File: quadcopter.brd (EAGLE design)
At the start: 138 x 138 mm, 65 parts, among them J1 AVR_SPI_PRG_6NS, Q1 N-CHANNEL_MOSFET, Q2 N-CHANNEL_MOSFET, Q3 N-CHANNEL_MOSFET, Q4 N-CHANNEL_MOSFET, U1 ATMEGA128RFA1

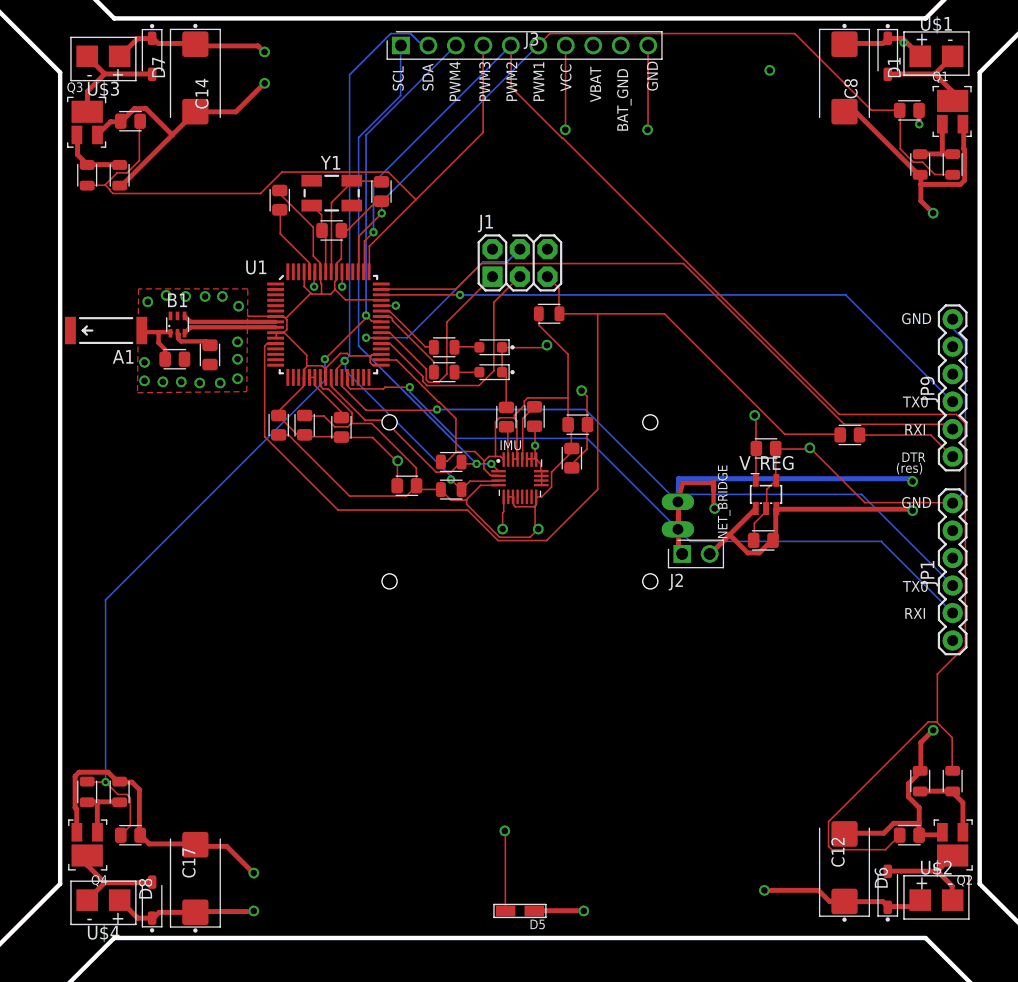
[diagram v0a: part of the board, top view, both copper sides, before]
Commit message: Changed ground on LED to batgnd"
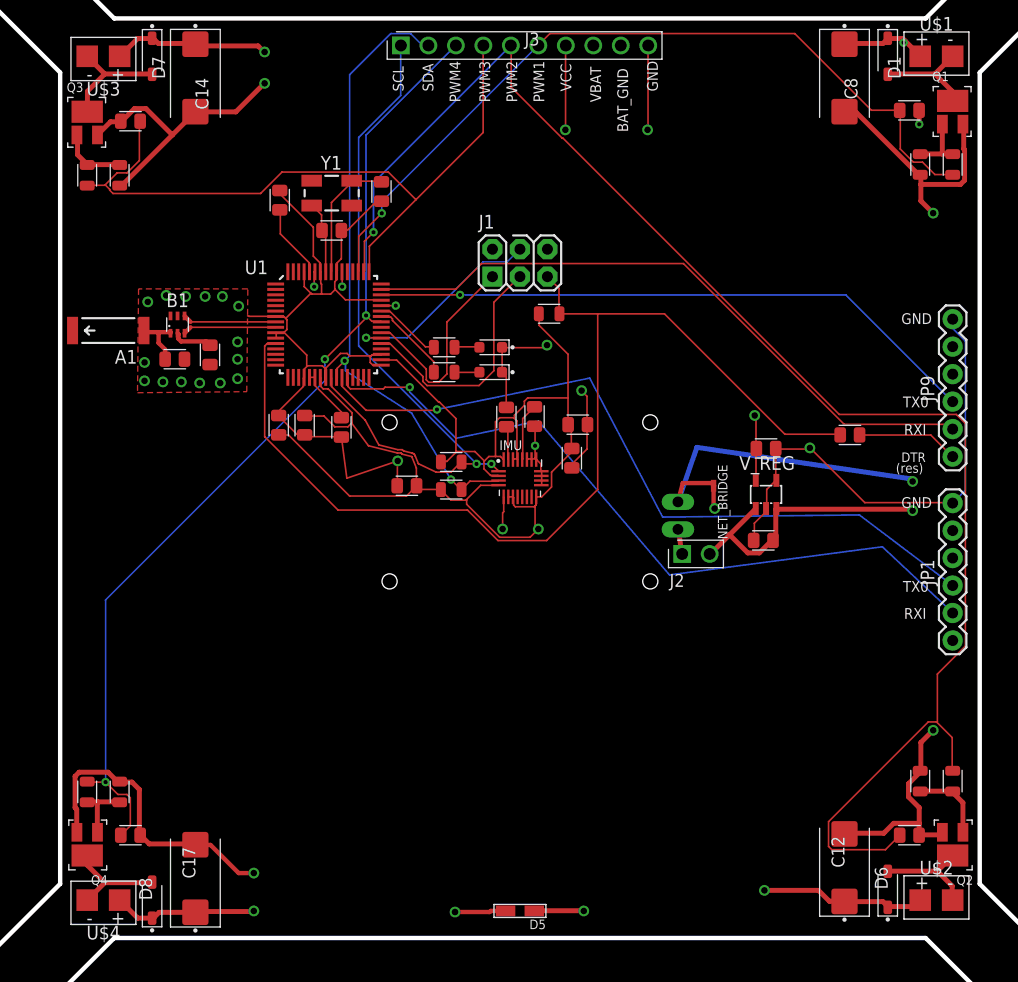
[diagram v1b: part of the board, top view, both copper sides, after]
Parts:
- moved A1 0.20 mm to (31.9, 83.7)
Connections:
- net BAT_GND: now also D5.P$2
- net GND: no longer D5.P$2
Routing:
- net BAT_GND: track 127.9 -> 134.3 mm, vias 6 -> 7
- net GND: track 167.0 -> 162.4 mm, vias 24 -> 23
- net N$18: track 6.75 -> 2.35 mm
- net N$9: track 65.0 -> 68.5 mm
- net N$12: track 65.8 -> 68.5 mm
- net SDA: track 58.0 -> 58.6 mm
- net VBAT: vias 7 -> 6

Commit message: Board passes DFM
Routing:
- net GND: track 162.4 -> 264.8 mm, vias 23 -> 16
- net RESET: track 96.9 -> 62.3 mm, vias 0 -> 1
- net VBAT: track 84.6 -> 110.8 mm, vias 6 -> 5
- net SDA: track 58.6 -> 81.7 mm
- net VCC: track 134.6 -> 111.9 mm, vias 6 -> 7
- net PWM3: track 65.7 -> 78.3 mm
- net SCL: track 65.4 -> 53.0 mm, vias 2 -> 1
- net PWM2: track 142.5 -> 131.5 mm
- net PWM4: track 91.7 -> 101.6 mm, vias 3 -> 2
- net MOSI: track 19.0 -> 27.8 mm
- net BAT_GND: track 134.3 -> 141.6 mm, vias 7 -> 8
- net MISO: track 19.6 -> 12.4 mm, vias 0 -> 2
- net RX0: track 56.9 -> 63.5 mm
- net PWM1: track 74.0 -> 78.4 mm
- net N$12: track 68.5 -> 65.6 mm
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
